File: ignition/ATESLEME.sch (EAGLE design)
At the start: 54 parts, among them U1 ADXL345PATRICK, U7 AMS1117-3.3

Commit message: Discrite polygon was applied to heat pad of AMS1117-3.3
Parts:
- removed U7: AMS1117-3.3, AMS1117-3.3:AMS1117-3.3
- added U3: AMS1117-3.3, AMS1117-3.3:AMS1117-3.3
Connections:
- new net HT: U3.HT
- net GND: now also U3.ADJ; no longer U7.ADJ/GND
- net N$1: now also U3.VOUT; no longer U7.VOUT
- net VNR: now also U3.VIN; no longer U7.VIN
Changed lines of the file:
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@@
 <part name="SW" library="SparkFun-Connectors" library_urn="urn:adsk.eagle:library:513" deviceset="CONN_02" device="3.5MM-NO_SILK" package3d_urn="urn:adsk.eagle:package:38055/1"/>
 <part name="OSC" library="ABMM2-8.000MHZ-E2-T" deviceset="ABMM2-8.000MHZ-E2-T" device=""/>
-<part name="U7" library="AMS1117-3.3" deviceset="AMS1117-3.3" device=""/>
 <part name="RC4" library="SparkFun-Capacitors" library_urn="urn:adsk.eagle:library:510" deviceset="10UF-POLAR" device="-EIA3528-20V-10%(TANT)" package3d_urn="urn:adsk.eagle:package:37411/1" value="22uF"/>
 <part name="RC3" library="SparkFun-Capacitors" library_urn="urn:adsk.eagle:library:510" deviceset="0.1UF" device="-0603-25V-(+80/-20%)" package3d_urn="urn:adsk.eagle:package:37414/1" value="100nF"/>
@@
 <part name="U$2" library="SparkFun-PowerSymbols" library_urn="urn:adsk.eagle:library:530" deviceset="VDDA" device=""/>
 <part name="LS1" library="SparkFun-Electromechanical" library_urn="urn:adsk.eagle:library:516" deviceset="BUZZER" device="-PTH" package3d_urn="urn:adsk.eagle:package:38558/1"/>
+<part name="U3" library="AMS1117-3.3" library_urn="urn:adsk.eagle:library:27162810" deviceset="AMS1117-3.3" device="" package3d_urn="urn:adsk.eagle:package:27162813/2"/>
 </parts>
 <sheets>
@@
 <attribute name="VALUE" x="469.8746" y="108.6104" size="0.508" layer="96" rot="R180"/>
 </instance>
-<instance part="U7" gate="G$1" x="424.18" y="167.64" smashed="yes">
-<attribute name="NAME" x="414.0034" y="173.237140625" size="2.54415" layer="95"/>
-<attribute name="VALUE" x="414.0108" y="159.504640625" size="2.5423" layer="96"/>
-</instance>
 <instance part="RC4" gate="G$1" x="462.28" y="165.1" smashed="yes">
 <attribute name="NAME" x="463.296" y="165.735" size="1.778" layer="95" font="vector"/>
@@
 <attribute name="NAME" x="469.9" y="53.086" size="1.778" layer="95" font="vector"/>
 </instance>
+<instance part="U3" gate="G$1" x="421.64" y="167.64" smashed="yes">
+<attribute name="NAME" x="416.7974" y="173.491140625" size="1.4224" layer="95"/>
+<attribute name="VALUE" x="416.8048" y="160.774640625" size="1.4224" layer="96"/>
+</instance>
 </instances>
 <busses>
@@
 <wire x1="388.62" y1="157.48" x2="401.32" y2="157.48" width="0.1524" layer="91"/>
 <pinref part="RC2" gate="G$1" pin="2"/>
-<wire x1="401.32" y1="157.48" x2="439.42" y2="157.48" width="0.1524" layer="91"/>
+<wire x1="401.32" y1="157.48" x2="424.18" y2="157.48" width="0.1524" layer="91"/>
+<wire x1="424.18" y1="157.48" x2="439.42" y2="157.48" width="0.1524" layer="91"/>
 <wire x1="401.32" y1="160.02" x2="401.32" y2="157.48" width="0.1524" layer="91"/>
 <junction x="401.32" y="157.48"/>
-<pinref part="U7" gate="G$1" pin="ADJ/GND"/>
-<wire x1="439.42" y1="165.1" x2="439.42" y2="157.48" width="0.1524" layer="91"/>
-<junction x="439.42" y="157.48"/>
 <pinref part="RC3" gate="G$1" pin="2"/>
 <wire x1="439.42" y1="157.48" x2="449.58" y2="157.48" width="0.1524" layer="91"/>
@@
 <wire x1="469.9" y1="157.48" x2="462.28" y2="157.48" width="0.1524" layer="91"/>
 <junction x="462.28" y="157.48"/>
+<pinref part="U3" gate="G$1" pin="ADJ"/>
+<junction x="424.18" y="157.48"/>
 </segment>
 <segment>
@@
 <net name="VNR" class="0">
 <segment>
-<pinref part="U7" gate="G$1" pin="VIN"/>
 <pinref part="RC1" gate="G$1" pin="+"/>
-<wire x1="408.94" y1="170.18" x2="401.32" y2="170.18" width="0.1524" layer="91"/>
 <wire x1="401.32" y1="170.18" x2="388.62" y2="170.18" width="0.1524" layer="91"/>
 <wire x1="388.62" y1="167.64" x2="388.62" y2="170.18" width="0.1524" layer="91"/>
 <pinref part="RC2" gate="G$1" pin="1"/>
 <wire x1="401.32" y1="167.64" x2="401.32" y2="170.18" width="0.1524" layer="91"/>
-<junction x="401.32" y="170.18"/>
 <pinref part="RGD" gate="G$1" pin="C"/>
 <wire x1="386.08" y1="170.18" x2="388.62" y2="170.18" width="0.1524" layer="91"/>
 <junction x="388.62" y="170.18"/>
+<pinref part="U3" gate="G$1" pin="VIN"/>
+<junction x="401.32" y="170.18"/>
+<wire x1="411.48" y1="170.18" x2="401.32" y2="170.18" width="0.1524" layer="91"/>
 </segment>
 </net>
 <net name="N$1" class="0">
 <segment>
-<pinref part="U7" gate="G$1" pin="VOUT"/>
 <pinref part="RC4" gate="G$1" pin="+"/>
-<wire x1="439.42" y1="170.18" x2="449.58" y2="170.18" width="0.1524" layer="91"/>
 <wire x1="449.58" y1="170.18" x2="462.28" y2="170.18" width="0.1524" layer="91"/>
 <wire x1="462.28" y1="170.18" x2="462.28" y2="167.64" width="0.1524" layer="91"/>
 <pinref part="RC3" gate="G$1" pin="1"/>
 <wire x1="449.58" y1="167.64" x2="449.58" y2="170.18" width="0.1524" layer="91"/>
-<junction x="449.58" y="170.18"/>
 <pinref part="F" gate="G$1" pin="1"/>
 <wire x1="467.36" y1="170.18" x2="462.28" y2="170.18" width="0.1524" layer="91"/>
 <junction x="462.28" y="170.18"/>
+<pinref part="U3" gate="G$1" pin="VOUT"/>
+<wire x1="436.88" y1="170.18" x2="449.58" y2="170.18" width="0.1524" layer="91"/>
+<junction x="449.58" y="170.18"/>
 </segment>
 </net>
@@
 </segment>
 </net>
+<net name="HT" class="0">
+<segment>
+<pinref part="U3" gate="G$1" pin="HT"/>
+<wire x1="411.48" y1="165.1" x2="408.94" y2="165.1" width="0.1524" layer="91"/>
+<label x="408.94" y="165.1" size="1.778" layer="95" rot="R90" xref="yes"/>
+</segment>
+</net>

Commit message: Telemetry V1.0.0 was completed
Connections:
- new net IN1: U1.INT1, U2A.PB9
- new net IN2: U1.INT2, U2A.PB8
- new net INT1: LPS-1.INT1, U2A.PB5
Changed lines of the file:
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@@
+</segment>
+</net>
+<net name="INT1" class="0">
+<segment>
+<pinref part="U2" gate="A" pin="PB5"/>
+<wire x1="314.96" y1="22.86" x2="309.88" y2="22.86" width="0.1524" layer="91"/>
+<label x="309.88" y="22.86" size="1.27" layer="95" rot="R180" xref="yes"/>
+</segment>
+<segment>
+<pinref part="LPS-1" gate="G$1" pin="INT1"/>
+<wire x1="353.06" y1="154.94" x2="358.14" y2="154.94" width="0.1524" layer="91"/>
+<label x="358.14" y="154.94" size="1.27" layer="95" xref="yes"/>
+</segment>
+</net>
+<net name="IN1" class="0">
+<segment>
+<pinref part="U1" gate="G$1" pin="INT1"/>
+<wire x1="335.28" y1="99.06" x2="340.36" y2="99.06" width="0.1524" layer="91"/>
+<label x="340.36" y="99.06" size="1.27" layer="95" xref="yes"/>
+</segment>
+<segment>
+<pinref part="U2" gate="A" pin="PB9"/>
+<wire x1="314.96" y1="12.7" x2="309.88" y2="12.7" width="0.1524" layer="91"/>
+<label x="309.88" y="12.7" size="1.27" layer="95" rot="R180" xref="yes"/>
+</segment>
+</net>
+<net name="IN2" class="0">
+<segment>
+<pinref part="U1" gate="G$1" pin="INT2"/>
+<wire x1="335.28" y1="96.52" x2="340.36" y2="96.52" width="0.1524" layer="91"/>
+<label x="340.36" y="96.52" size="1.27" layer="95" xref="yes"/>
+</segment>
+<segment>
+<pinref part="U2" gate="A" pin="PB8"/>
+<wire x1="314.96" y1="15.24" x2="309.88" y2="15.24" width="0.1524" layer="91"/>
+<label x="309.88" y="15.24" size="1.27" layer="95" rot="R180" xref="yes"/>
 </segment>
 </net>

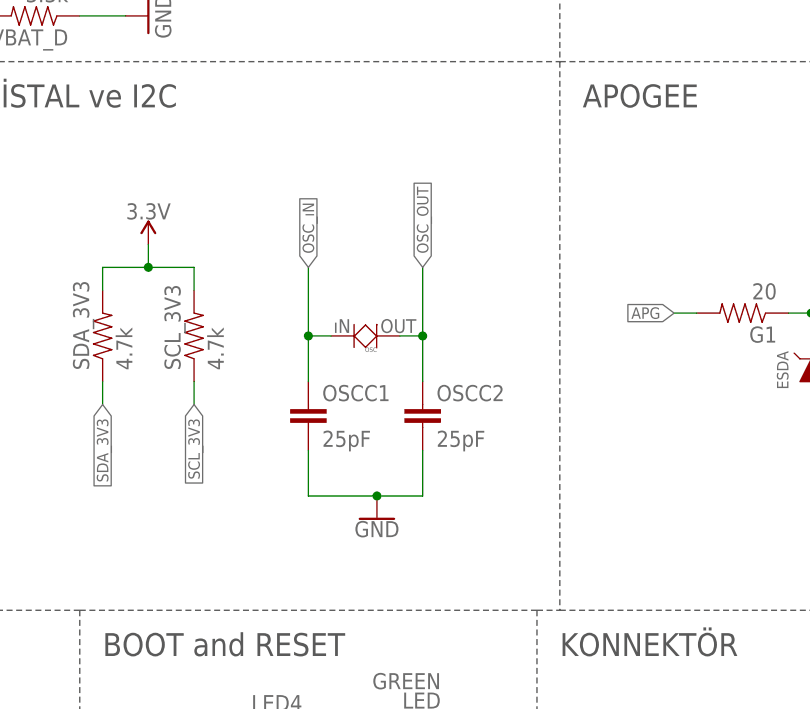
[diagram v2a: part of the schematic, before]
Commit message: Redesign was maken for ignition
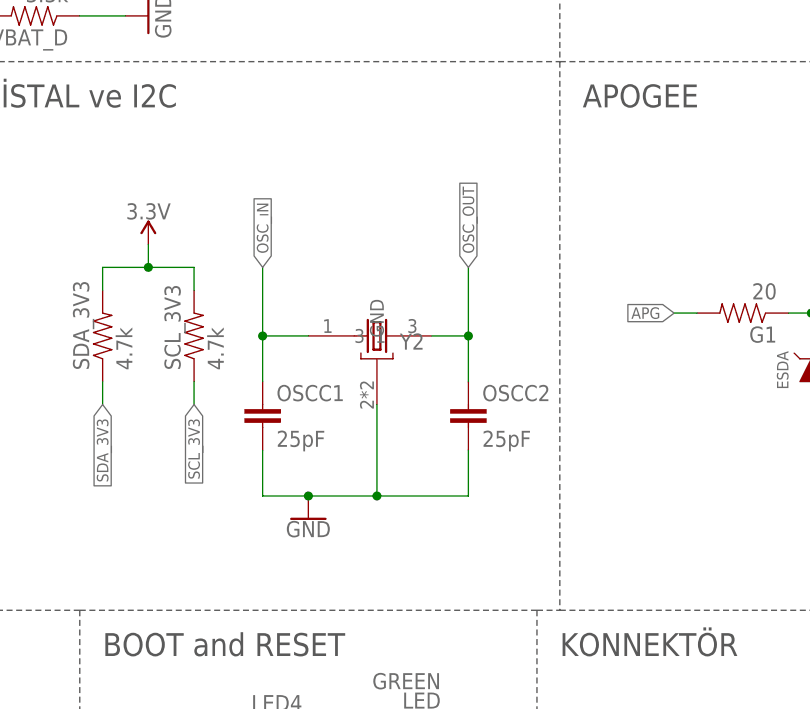
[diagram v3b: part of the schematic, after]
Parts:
- removed OSC: (no value), ABMM2-8.000MHZ-E2-T:ABMM2-8.000MHZ-E2-T
- added Y2: ABM2B-8.000MHZ-10-1-U-T, ABM3B-26.000MHZ-10-1-U-T:ABM3B-26.000MHZ-10-1-U-T
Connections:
- net GND: now also Y2.GND
- net OSC_OUT: now also Y2.3; no longer OSC.OUT
- net OSC_ıN: now also Y2.1; no longer OSC.IN
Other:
- moved on the sheet: OSCC1, OSCC2
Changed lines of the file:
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@@
 <layer number="56" name="wert" color="7" fill="1" visible="no" active="no"/>
 <layer number="57" name="tCAD" color="7" fill="1" visible="no" active="no"/>
+<layer number="58" name="bCAD" color="11" fill="1" visible="no" active="no"/>
 <layer number="59" name="tCarbon" color="7" fill="1" visible="no" active="no"/>
 <layer number="60" name="bCarbon" color="7" fill="1" visible="no" active="no"/>
@@
 <part name="SUPPLY4" library="SparkFun-PowerSymbols" library_urn="urn:adsk.eagle:library:530" deviceset="VCC" device="" value="VIN"/>
 <part name="SW" library="SparkFun-Connectors" library_urn="urn:adsk.eagle:library:513" deviceset="CONN_02" device="3.5MM-NO_SILK" package3d_urn="urn:adsk.eagle:package:38055/1"/>
-<part name="OSC" library="ABMM2-8.000MHZ-E2-T" deviceset="ABMM2-8.000MHZ-E2-T" device=""/>
 <part name="RC4" library="SparkFun-Capacitors" library_urn="urn:adsk.eagle:library:510" deviceset="10UF-POLAR" device="-EIA3528-20V-10%(TANT)" package3d_urn="urn:adsk.eagle:package:37411/1" value="22uF"/>
 <part name="RC3" library="SparkFun-Capacitors" library_urn="urn:adsk.eagle:library:510" deviceset="0.1UF" device="-0603-25V-(+80/-20%)" package3d_urn="urn:adsk.eagle:package:37414/1" value="100nF"/>
@@
 <part name="LS1" library="SparkFun-Electromechanical" library_urn="urn:adsk.eagle:library:516" deviceset="BUZZER" device="-PTH" package3d_urn="urn:adsk.eagle:package:38558/1"/>
 <part name="U3" library="AMS1117-3.3" library_urn="urn:adsk.eagle:library:27162810" deviceset="AMS1117-3.3" device="" package3d_urn="urn:adsk.eagle:package:27162813/2"/>
+<part name="Y2" library="ABM3B-26.000MHZ-10-1-U-T" deviceset="ABM3B-26.000MHZ-10-1-U-T" device="" value="ABM2B-8.000MHZ-10-1-U-T"/>
 </parts>
 <sheets>
@@
 <attribute name="NAME" x="520.7" y="61.468" size="1.778" layer="95" font="vector"/>
 </instance>
-<instance part="OSC" gate="G$1" x="469.9" y="107.95" smashed="yes" rot="R180">
-<attribute name="NAME" x="469.9" y="105.41" size="0.508" layer="95" rot="R180"/>
-<attribute name="VALUE" x="469.8746" y="108.6104" size="0.508" layer="96" rot="R180"/>
-</instance>
 <instance part="RC4" gate="G$1" x="462.28" y="165.1" smashed="yes">
 <attribute name="NAME" x="463.296" y="165.735" size="1.778" layer="95" font="vector"/>
@@
 <attribute name="VALUE" x="449.58" y="12.446" size="1.778" layer="96" align="top-center"/>
 </instance>
-<instance part="OSCC1" gate="G$1" x="462.28" y="96.52" smashed="yes">
-<attribute name="NAME" x="463.804" y="99.441" size="1.778" layer="95" font="vector"/>
-<attribute name="VALUE" x="463.804" y="94.361" size="1.778" layer="96" font="vector"/>
-</instance>
-<instance part="OSCC2" gate="G$1" x="474.98" y="96.52" smashed="yes">
-<attribute name="NAME" x="476.504" y="99.441" size="1.778" layer="95" font="vector"/>
-<attribute name="VALUE" x="476.504" y="94.361" size="1.778" layer="96" font="vector"/>
-</instance>
-<instance part="GND14" gate="1" x="469.9" y="86.36" smashed="yes">
-<attribute name="VALUE" x="469.9" y="86.106" size="1.778" layer="96" align="top-center"/>
+<instance part="OSCC1" gate="G$1" x="457.2" y="96.52" smashed="yes">
+<attribute name="NAME" x="458.724" y="99.441" size="1.778" layer="95" font="vector"/>
+<attribute name="VALUE" x="458.724" y="94.361" size="1.778" layer="96" font="vector"/>
+</instance>
+<instance part="OSCC2" gate="G$1" x="480.06" y="96.52" smashed="yes">
+<attribute name="NAME" x="481.584" y="99.441" size="1.778" layer="95" font="vector"/>
+<attribute name="VALUE" x="481.584" y="94.361" size="1.778" layer="96" font="vector"/>
+</instance>
+<instance part="GND14" gate="1" x="462.28" y="86.36" smashed="yes">
+<attribute name="VALUE" x="462.28" y="86.106" size="1.778" layer="96" align="top-center"/>
 </instance>
 <instance part="LED4" gate="G$1" x="459.74" y="63.5" smashed="yes">
@@
 <attribute name="NAME" x="416.7974" y="173.491140625" size="1.4224" layer="95"/>
 <attribute name="VALUE" x="416.8048" y="160.774640625" size="1.4224" layer="96"/>
+</instance>
+<instance part="Y2" gate="G$1" x="469.9" y="106.68" smashed="yes">
+<attribute name="NAME" x="472.445409375" y="105.15816875" size="1.781790625" layer="95"/>
 </instance>
 </instances>
@@
 <segment>
 <pinref part="OSCC2" gate="G$1" pin="2"/>
-<wire x1="474.98" y1="93.98" x2="474.98" y2="88.9" width="0.1524" layer="91"/>
+<wire x1="480.06" y1="93.98" x2="480.06" y2="88.9" width="0.1524" layer="91"/>
 <pinref part="GND14" gate="1" pin="GND"/>
-<wire x1="474.98" y1="88.9" x2="469.9" y2="88.9" width="0.1524" layer="91"/>
+<wire x1="480.06" y1="88.9" x2="469.9" y2="88.9" width="0.1524" layer="91"/>
 <wire x1="469.9" y1="88.9" x2="462.28" y2="88.9" width="0.1524" layer="91"/>
+<wire x1="462.28" y1="88.9" x2="457.2" y2="88.9" width="0.1524" layer="91"/>
+<junction x="462.28" y="88.9"/>
+<pinref part="OSCC1" gate="G$1" pin="2"/>
+<wire x1="457.2" y1="88.9" x2="457.2" y2="93.98" width="0.1524" layer="91"/>
+<pinref part="Y2" gate="G$1" pin="GND"/>
+<wire x1="469.9" y1="99.06" x2="469.9" y2="88.9" width="0.1524" layer="91"/>
 <junction x="469.9" y="88.9"/>
-<pinref part="OSCC1" gate="G$1" pin="2"/>
-<wire x1="462.28" y1="88.9" x2="462.28" y2="93.98" width="0.1524" layer="91"/>
 </segment>
 <segment>
@@
 </segment>
 <segment>
-<pinref part="OSC" gate="G$1" pin="IN"/>
-<wire x1="464.82" y1="106.68" x2="462.28" y2="106.68" width="0.1524" layer="91"/>
-<wire x1="462.28" y1="106.68" x2="462.28" y2="114.3" width="0.1524" layer="91"/>
+<wire x1="457.2" y1="101.6" x2="457.2" y2="106.68" width="0.1524" layer="91"/>
 <pinref part="OSCC1" gate="G$1" pin="1"/>
-<wire x1="462.28" y1="101.6" x2="462.28" y2="106.68" width="0.1524" layer="91"/>
-<junction x="462.28" y="106.68"/>
-<label x="462.28" y="114.3" size="1.27" layer="95" rot="R90" xref="yes"/>
+<label x="457.2" y="114.3" size="1.27" layer="95" rot="R90" xref="yes"/>
+<pinref part="Y2" gate="G$1" pin="1"/>
+<wire x1="457.2" y1="106.68" x2="457.2" y2="114.3" width="0.1524" layer="91"/>
+<wire x1="462.28" y1="106.68" x2="457.2" y2="106.68" width="0.1524" layer="91"/>
+<junction x="457.2" y="106.68"/>
 </segment>
 </net>
@@
 </segment>
 <segment>
-<pinref part="OSC" gate="G$1" pin="OUT"/>
-<wire x1="472.44" y1="106.68" x2="474.98" y2="106.68" width="0.1524" layer="91"/>
-<wire x1="474.98" y1="106.68" x2="474.98" y2="114.3" width="0.1524" layer="91"/>
+<wire x1="480.06" y1="101.6" x2="480.06" y2="106.68" width="0.1524" layer="91"/>
 <pinref part="OSCC2" gate="G$1" pin="1"/>
-<wire x1="474.98" y1="101.6" x2="474.98" y2="106.68" width="0.1524" layer="91"/>
-<junction x="474.98" y="106.68"/>
-<label x="474.98" y="114.3" size="1.27" layer="95" rot="R90" xref="yes"/>
+<label x="480.06" y="114.3" size="1.27" layer="95" rot="R90" xref="yes"/>
+<pinref part="Y2" gate="G$1" pin="3"/>
+<wire x1="480.06" y1="106.68" x2="480.06" y2="114.3" width="0.1524" layer="91"/>
+<wire x1="475.996" y1="106.68" x2="480.06" y2="106.68" width="0.1524" layer="91"/>
+<junction x="480.06" y="106.68"/>
 </segment>
 </net>
